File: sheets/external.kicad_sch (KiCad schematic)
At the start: 11 parts, among them CN3 STE_I2C_QT, J10 USART3, J11 Conn_01x04_Pin, J12 Airbrake_Pot1, J13 Airbrake_Pot2, J14 SPARE_ADC1, J15 SPARE_ADC2, J8 Conn_01x03_Pin, J9 Conn_01x03_Pin

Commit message: added spi
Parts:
- removed J15: SPARE_ADC2, symbol Connector:Conn_01x03_Pin
- added J15, J16: Conn_01x05_Pin, symbol Connector:Conn_01x05_Pin
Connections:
- net +3V3: now also J15.5 (Pin_5), J16.5 (Pin_5)
- net GND: now also J15.1 (Pin_1), J16.1 (Pin_1)
- new net SPI2.MISO: J16.3 (Pin_3)
- new net SPI2.MOSI: J16.2 (Pin_2)
- new net SPI2.SCK: J16.4 (Pin_4)
- new net SPI4.MISO: J15.3 (Pin_3)
- new net SPI4.MOSI: J15.2 (Pin_2)
- new net SPI4.SCK: J15.4 (Pin_4)
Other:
- moved on the sheet: J10

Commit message: added gpio connections in root, UART8, ADC2
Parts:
- added J1: UART8, symbol Connector:Conn_01x04_Pin
- added J17, J18: Conn_01x06_Pin, symbol Connector:Conn_01x06_Pin
- added J5: SPARE_ADC2, symbol Connector:Conn_01x03_Pin
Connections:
- net +3V3: now also J1.4 (Pin_4), J17.6 (Pin_6), J18.6 (Pin_6), J5.2 (Pin_2)
- net GND: now also J1.1 (Pin_1), J17.1 (Pin_1), J18.1 (Pin_1), J5.3 (Pin_3)
- net TARGET_RX renamed USART3_TARGET_RX
- net TARGET_TX renamed USART3_TARGET_TX
- new net PG10_IO: J17.2 (Pin_2)
- new net PG11_IO: J18.5 (Pin_5)
- new net PG12_IO: J18.4 (Pin_4)
- new net PG13_IO: J18.3 (Pin_3)
- new net PG14_IO: J18.2 (Pin_2)
- new net PG7_IO: J17.5 (Pin_5)
- new net PG8_IO: J17.4 (Pin_4)
- new net PG9_IO: J17.3 (Pin_3)
- new net SPARE_ADC2: J5.1 (Pin_1)
- new net UART8_TARGET_RX: J1.2 (Pin_2)
- new net UART8_TARGET_TX: J1.3 (Pin_3)
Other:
- note added: "GPIO"
- note added: "UART"

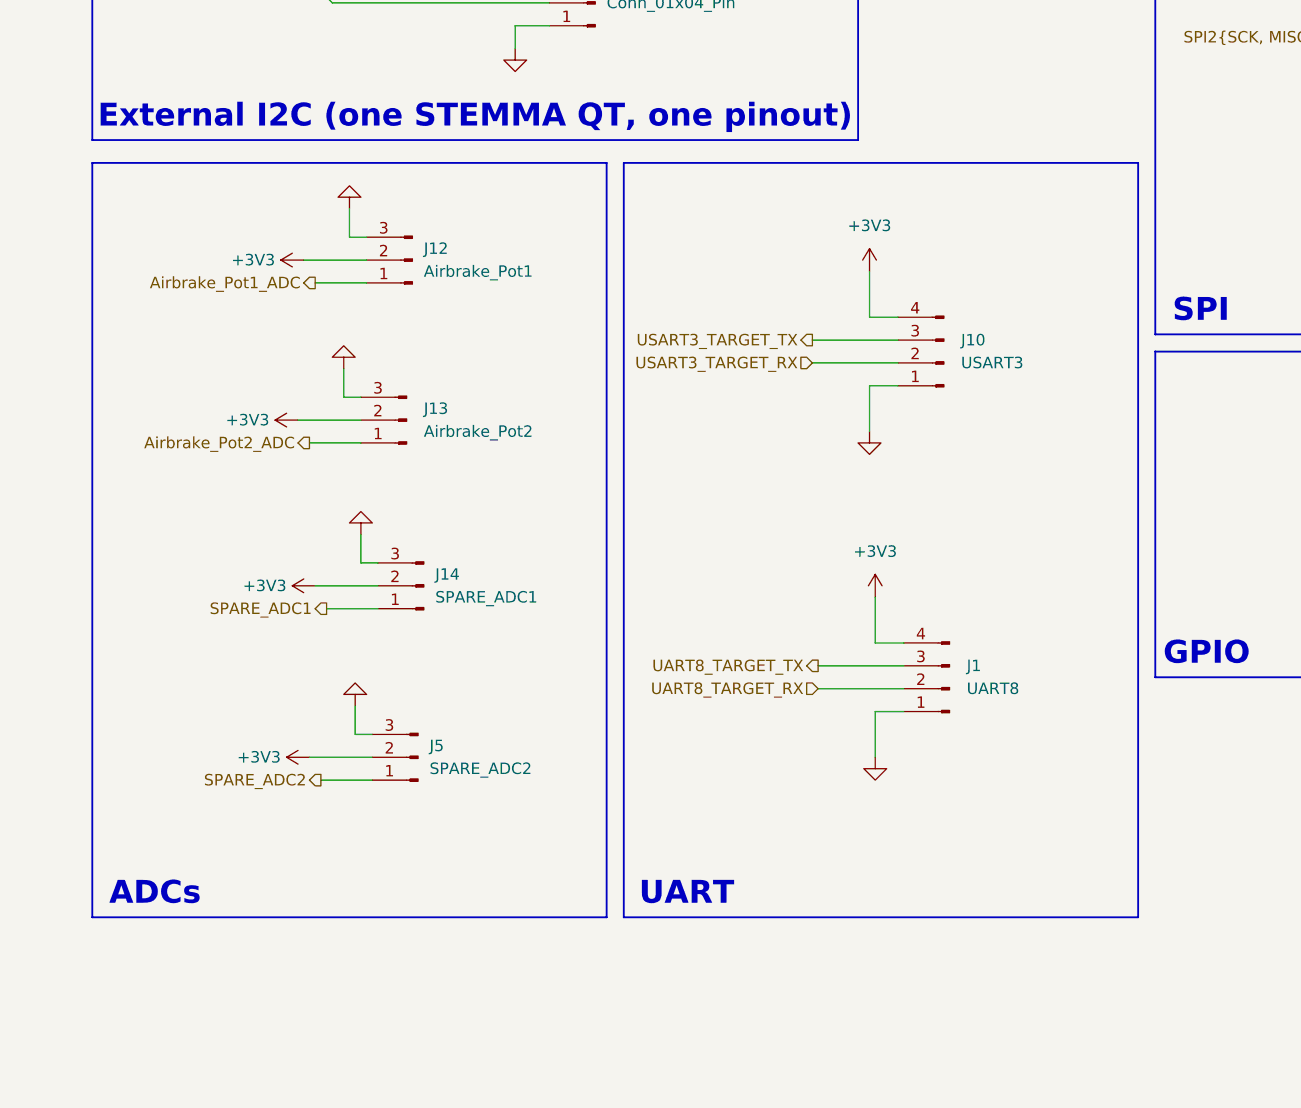
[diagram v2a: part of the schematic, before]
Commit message: final pwm channels added
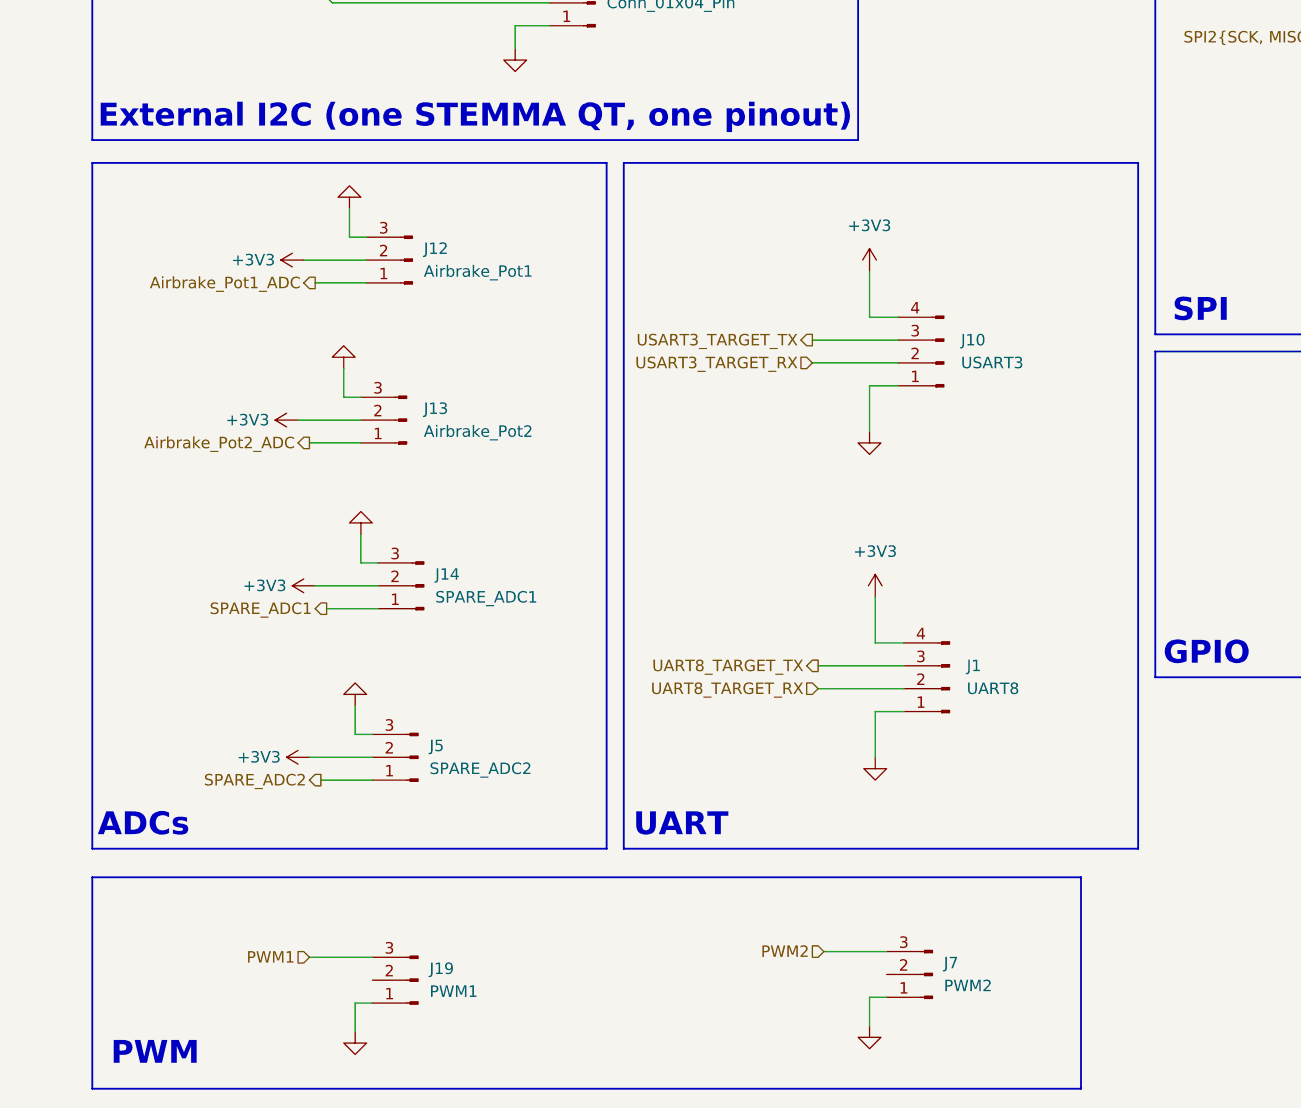
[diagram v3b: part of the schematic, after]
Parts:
- added J19: PWM1, symbol Connector:Conn_01x03_Pin
- added J7: PWM2, symbol Connector:Conn_01x03_Pin
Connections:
- net GND: now also J19.1 (Pin_1), J7.1 (Pin_1)
- new net PWM1: J19.3 (Pin_3)
- new net PWM2: J7.3 (Pin_3)
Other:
- note added: "PWM"

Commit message: Rev1 schematic done
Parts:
- removed CN3: STE_I2C_QT, easyeda2kicad:CONN-SMD_BM04B-SRSS-TB, symbol CONN-SMD_BM04B-SRSS-TB:BM04B-SRSS-TB(LF)(SN)
- added CN2: StemmaQT, aerolotl_custom:CONN-SMD_BM04B-SRSS-TB, symbol aerolotl_custom:StemmaQT
- renumbered F3 to F1, F4 to F2, J1 to J11, J8 to J12, J17 to J13, J16 to J14, J9 to J15, J18 to J16, J15 to J17, J13 to J3, J12 to J4, J19 to J6, J14 to J7, J11 to J8, J7 to J9
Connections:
- net +3V3: now also CN2.2
- net GND: now also CN2.0, CN2.1
- new net I2C2.SCL: CN2.4
- new net I2C2.SDA: CN2.3
- no-connect marks 0 -> 2
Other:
- moved on the sheet: F1, F2, J12, J13, J14, J15, J16, J17, J6, J8, J9

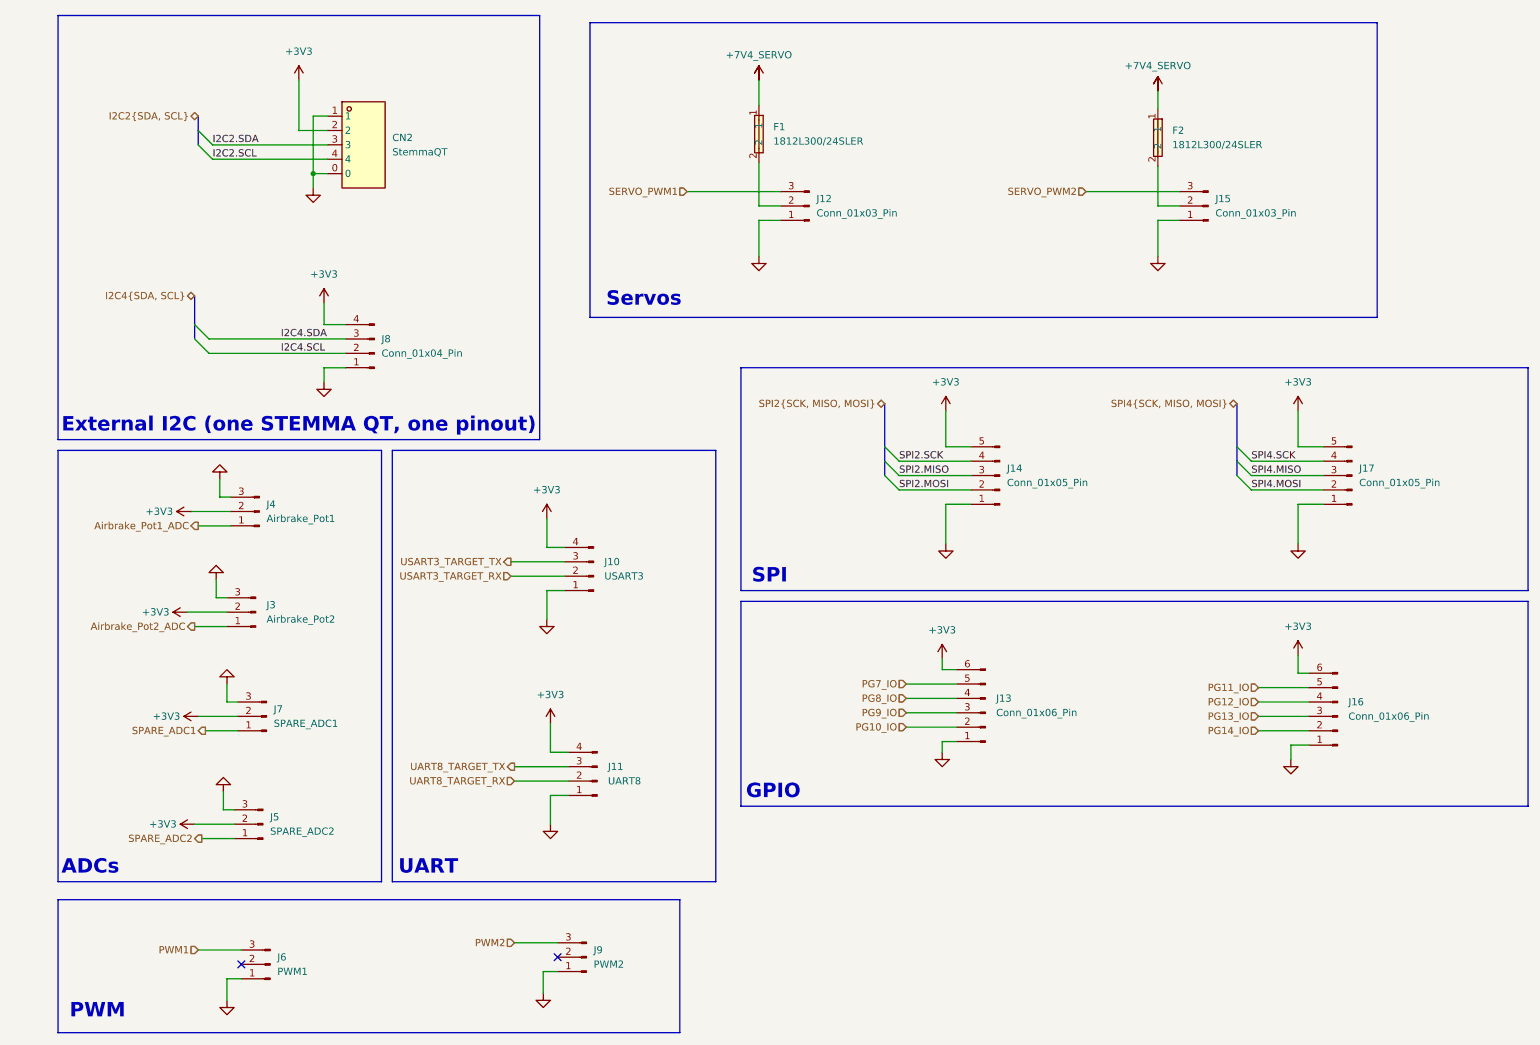
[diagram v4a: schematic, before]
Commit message: Cleared ALL ERC warnings
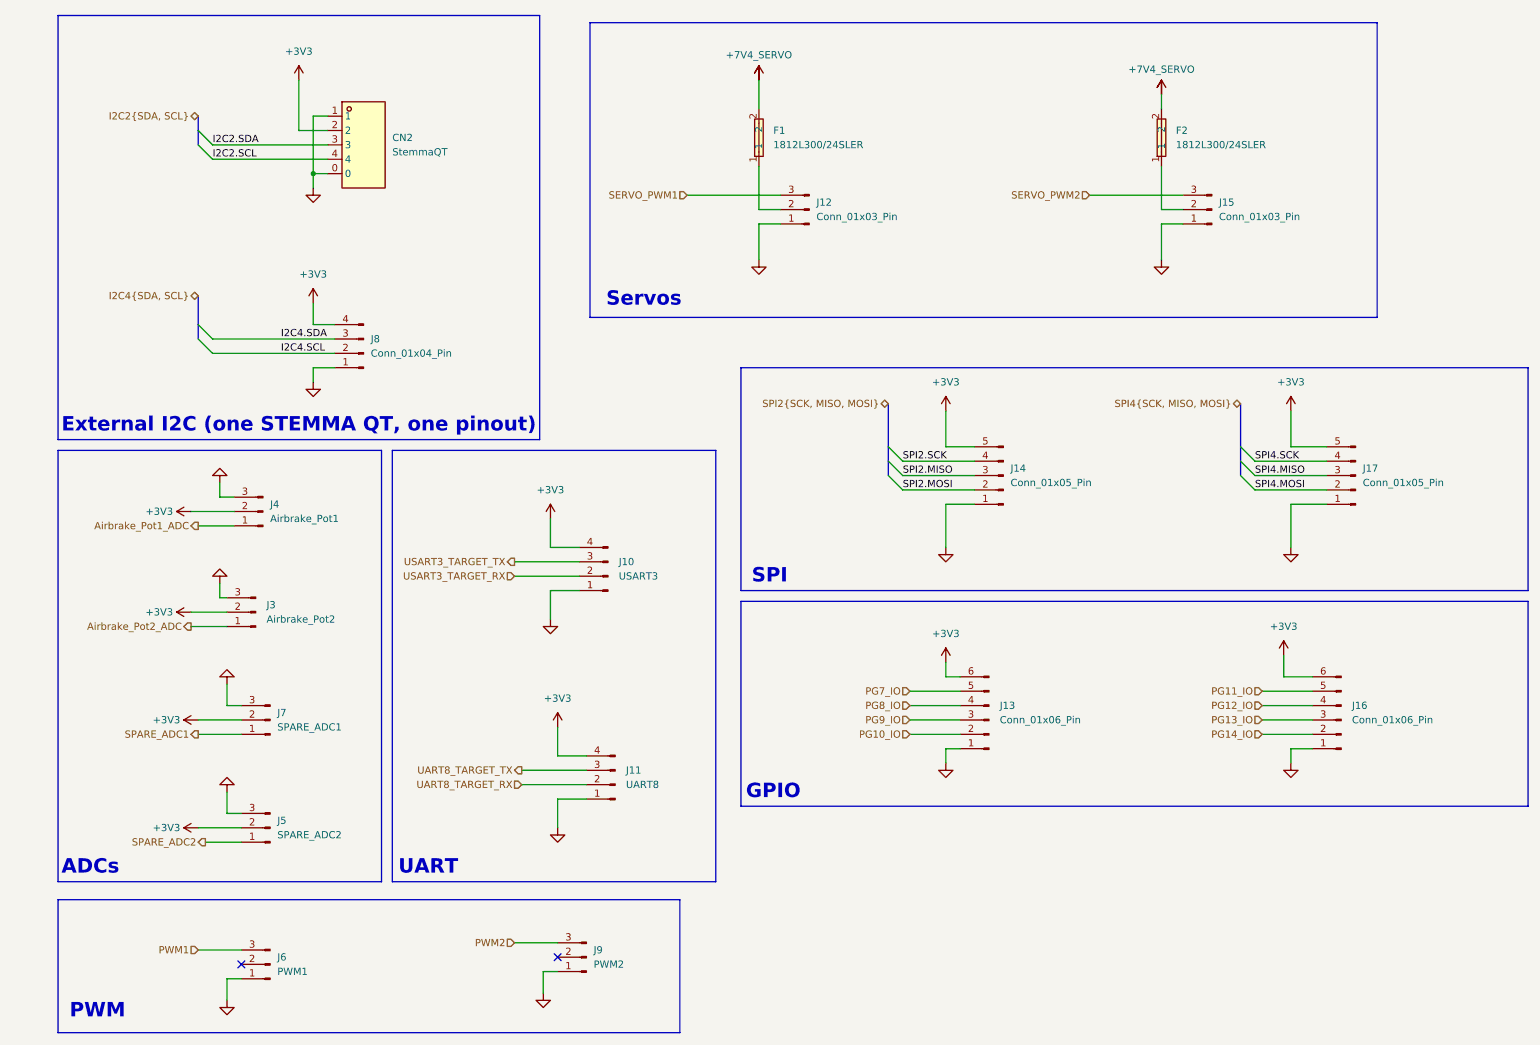
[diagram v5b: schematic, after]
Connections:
- net +7V4_SERVO: now also F1.2, F2.2; no longer F1.1, F2.1
- net at J12.2 (Pin_2): now also F1.1; no longer F1.2
- net at J15.2 (Pin_2): now also F2.1; no longer F2.2
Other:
- moved on the sheet: J10, J11, J12, J13, J14, J15, J16, J17, J4, J5, J7, J8

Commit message: some footprints assigned
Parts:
- F1: footprint aerolotl_custom:F1812 -> Capacitor_SMD:C_0402_1005Metric
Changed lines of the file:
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@@
 			)
 		)
-		(property "Footprint" "aerolotl_custom:F1812"
+		(property "Footprint" "Capacitor_SMD:C_0402_1005Metric"
 			(at 144.78 35.56 0)
 			(effects

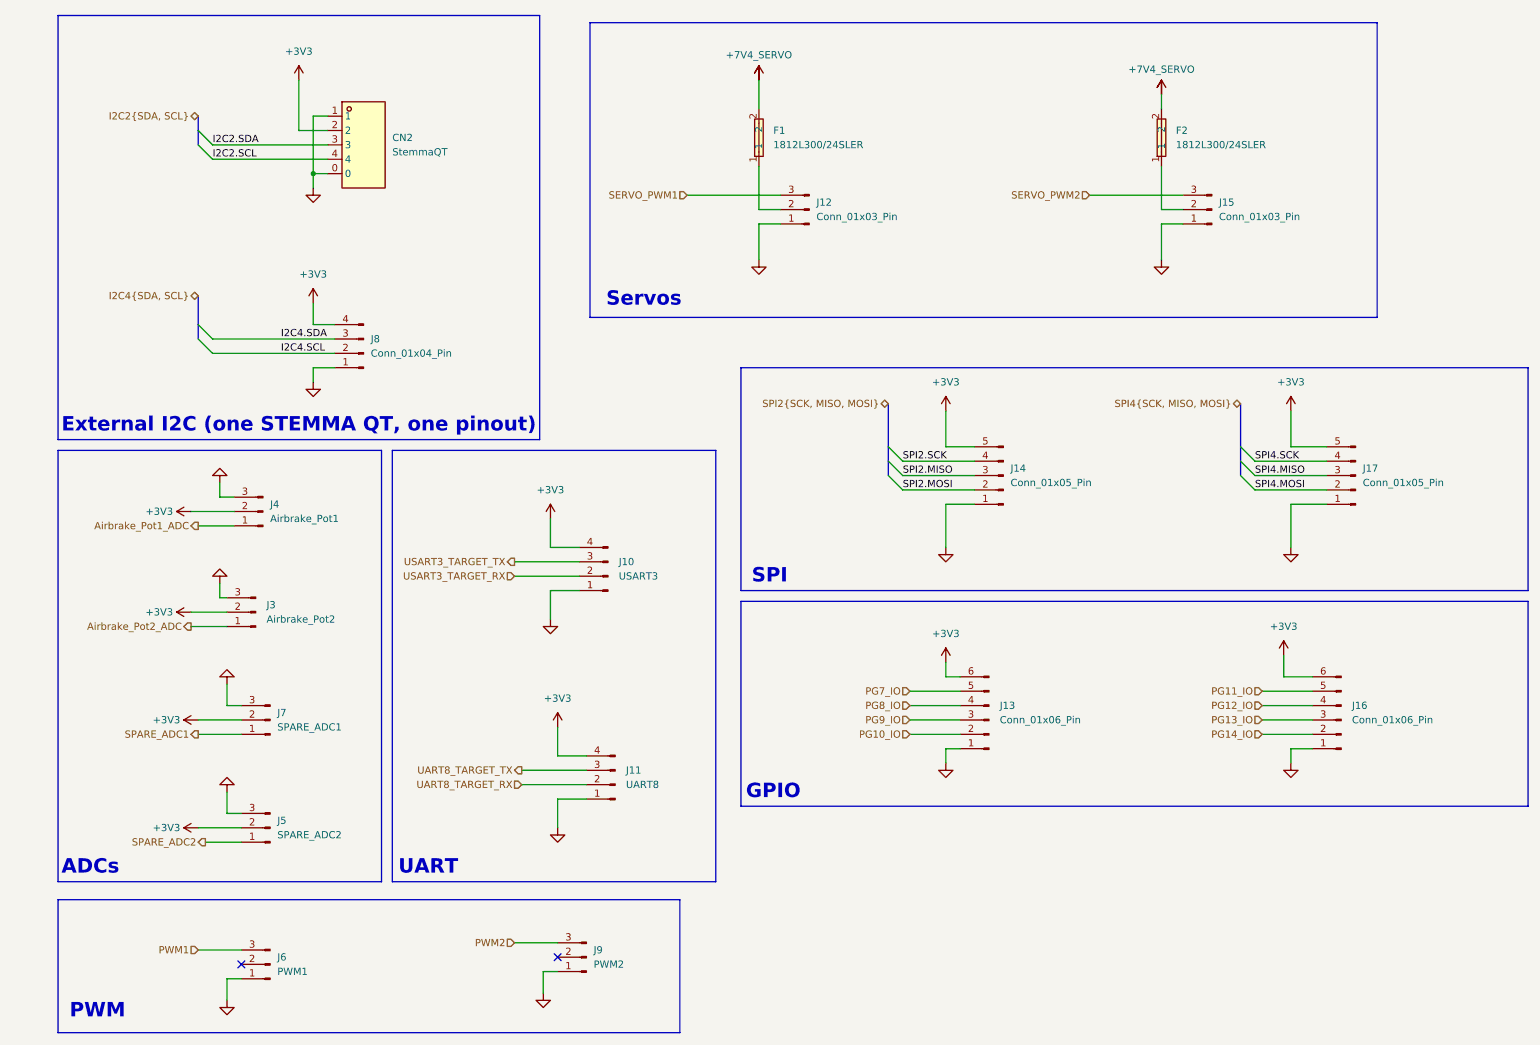
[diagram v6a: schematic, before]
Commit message: letter size schematic pages formatted
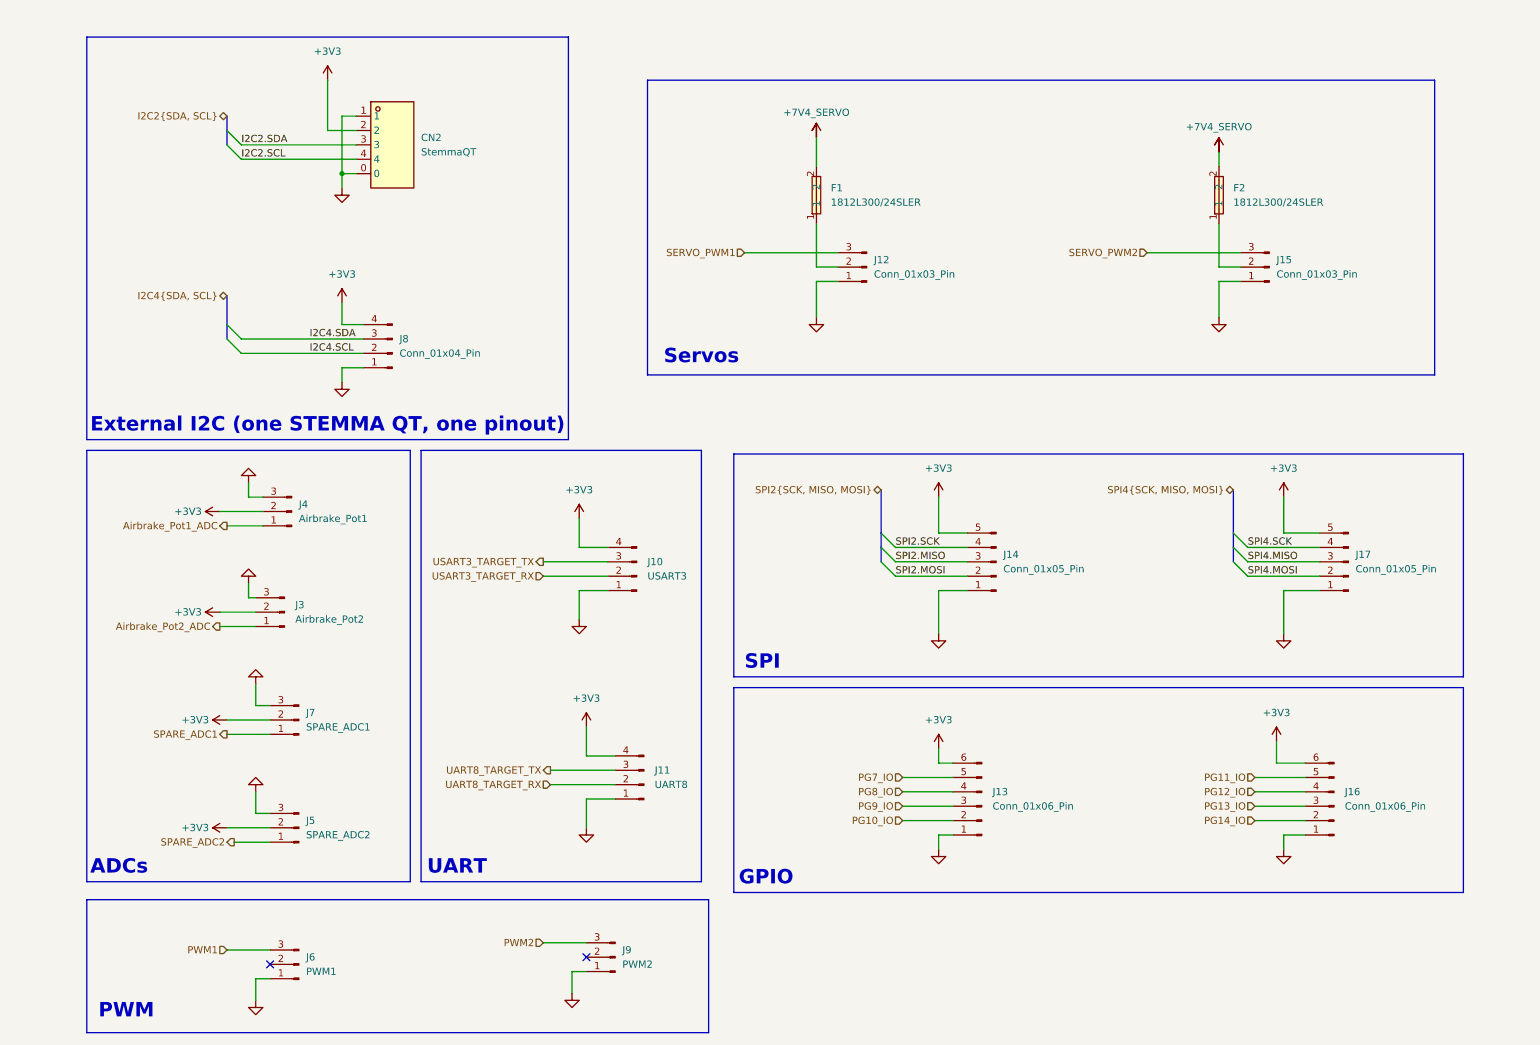
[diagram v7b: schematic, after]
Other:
- moved on the sheet: CN2, F1, F2, J10, J11, J12, J13, J14, J15, J16, J17, J3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
